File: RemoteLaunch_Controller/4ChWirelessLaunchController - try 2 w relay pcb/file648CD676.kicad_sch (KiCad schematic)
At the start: 24 parts, among them J1 Pad power and switch, J2 Control board, J3 Pad ch 1, J4 Pad ch 2, J5 Pad ch 3, J6 Pad ch 4, J7 Armed siren, J8 LED/Buzzer Continuity indicat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, J9 LED power indicator, K1 G2RL-2-DC24, K2 Ch 1 relay, K3 G8N-1U-DC12, K4 G8N-1U-DC12, K5 G8N-1U-DC12

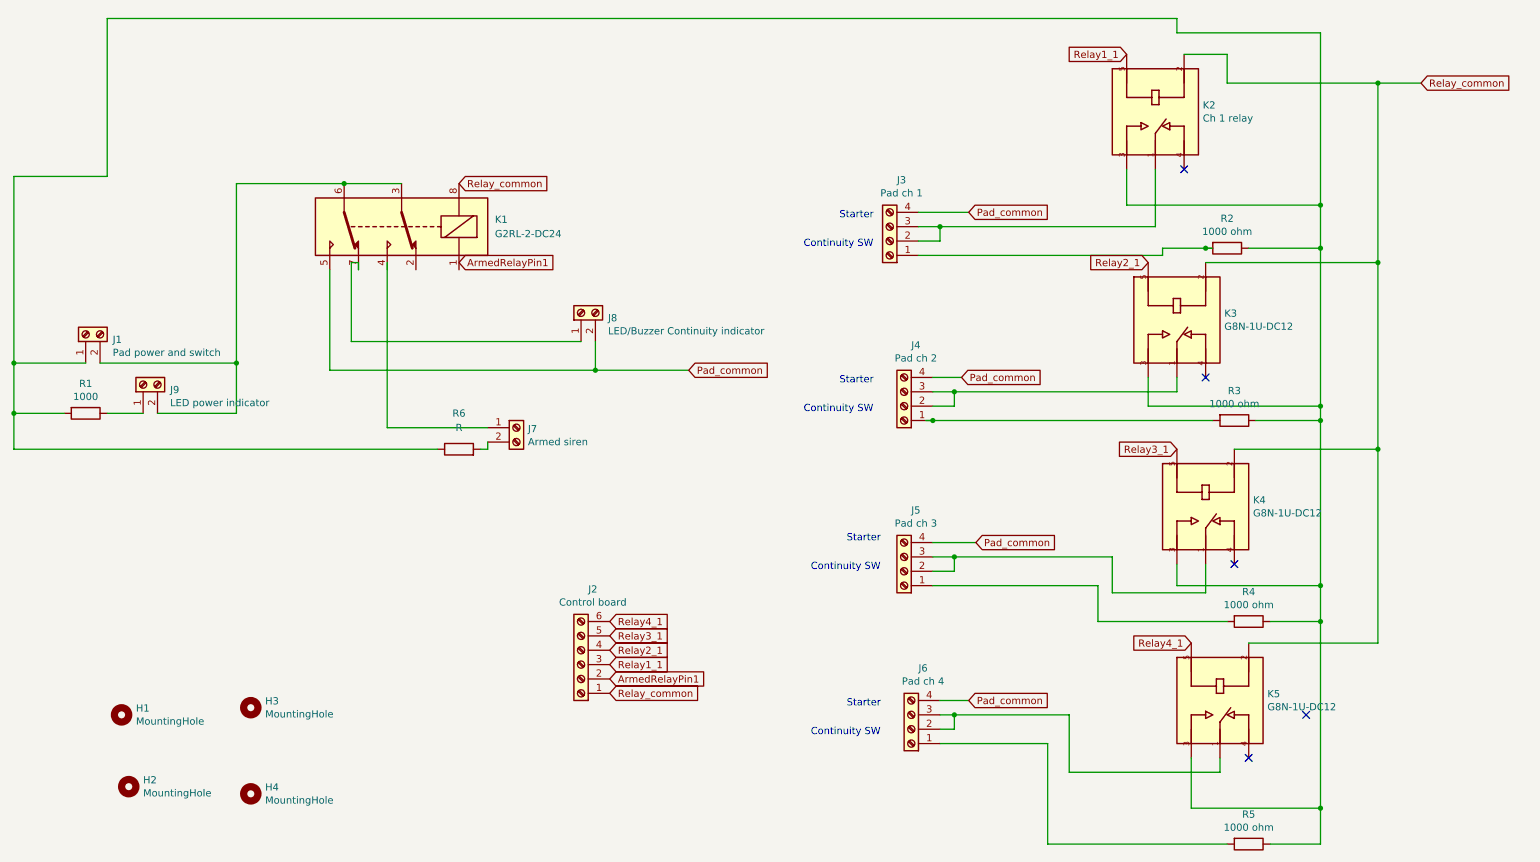
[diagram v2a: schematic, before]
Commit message: Working on adding polling / heartbeat;  Seem to have broken launch
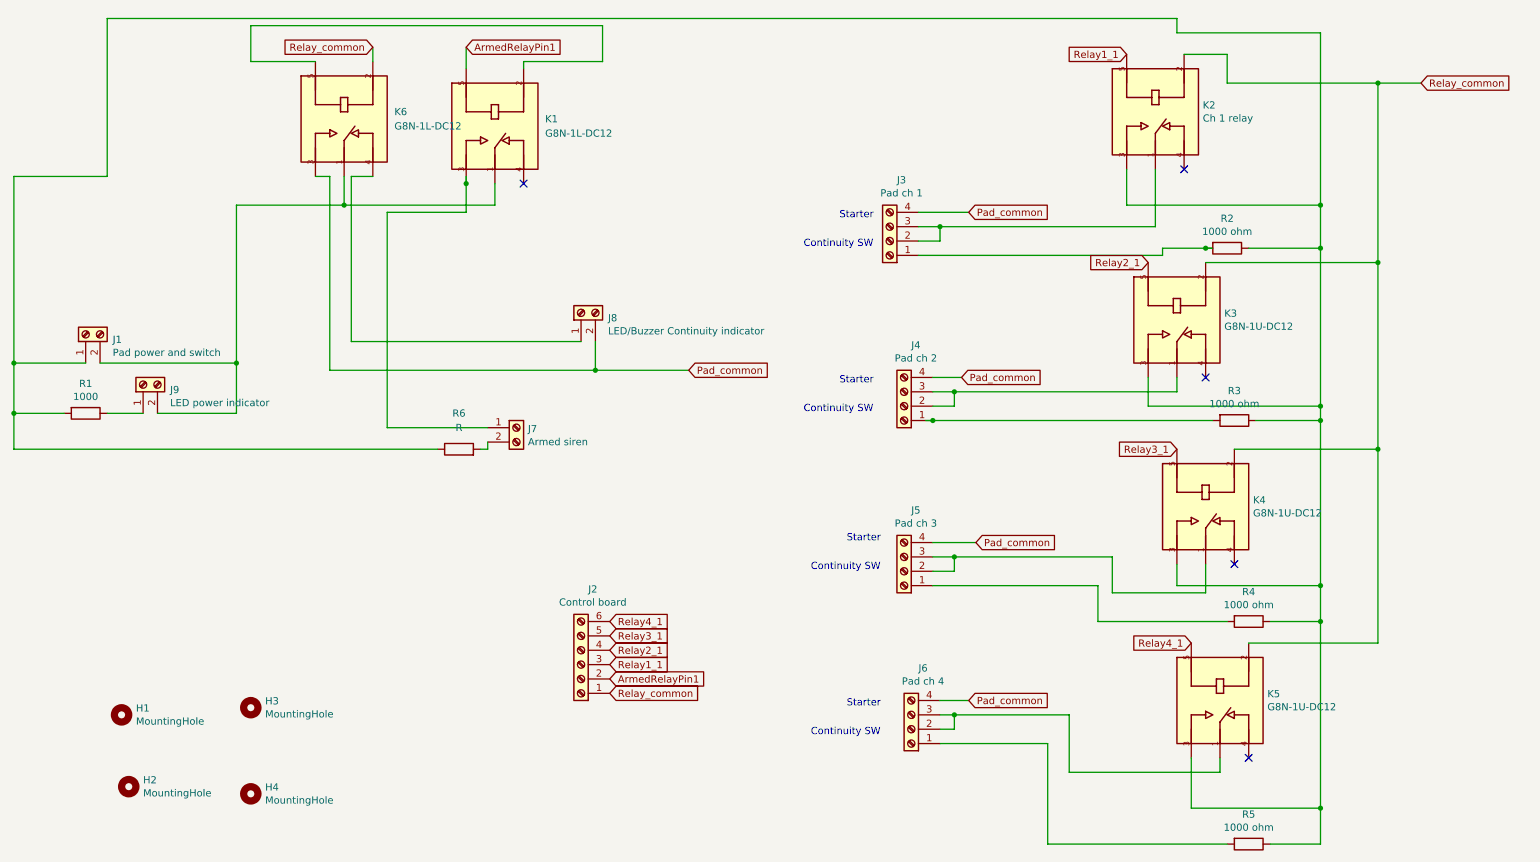
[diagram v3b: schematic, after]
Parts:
- removed K1: G2RL-2-DC24, Relay_THT:Relay_DPDT_Omron_G2RL, symbol Relay:G2RL-2-DC24
- added K1, K6: G8N-1L-DC12, RELAY_G8N-1U-DC12, symbol 4ChWirelessLaunchController-rescue:G8N-1U-DC12-G8N-1U-DC12
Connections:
- net ArmedRelayPin1: now also K1.5
- net Pad_common: now also K6.3
- net Relay_common: now also K6.2
- net at J1.2 (Pin_2), J9.2 (Pin_2): now also K1.1, K6.1
- net at J7.1 (Pin_1): now also K1.3
- net at J8.1 (Pin_1): now also K6.4
- new net: K1.2, K6.5
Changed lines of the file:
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@@
   (junction (at 255.27 29.21) (diameter 0) (color 0 0 0 0)
   )
-  (junction (at 72.39 46.99) (diameter 0) (color 0 0 0 0)
+  (junction (at 72.39 50.8) (diameter 0) (color 0 0 0 0)
+  )
+  (junction (at 93.98 46.99) (diameter 0) (color 0 0 0 0)
   )
   (junction (at 245.11 118.11) (diameter 0) (color 0 0 0 0)
@@
   (no_connect (at 232.41 148.59))
   (no_connect (at 229.87 114.3))
-  (no_connect (at 242.57 140.97))
   (no_connect (at 224.79 81.28))
+  (no_connect (at 104.14 46.99))
   (no_connect (at 220.98 44.45))
   (wire (pts (xy 245.11 157.48) (xy 245.11 163.83))
@@
     (stroke (width 0) (type default))
   )
+  (wire (pts (xy 77.47 22.86) (xy 77.47 25.4))
+    (stroke (width 0) (type default))
+  )
   (wire (pts (xy 13.97 78.74) (xy 13.97 87.63))
     (stroke (width 0) (type default))
@@
     (stroke (width 0) (type default))
   )
+  (wire (pts (xy 73.66 45.72) (xy 77.47 45.72))
+    (stroke (width 0) (type default))
+  )
   (wire (pts (xy 255.27 29.21) (xy 262.89 29.21))
     (stroke (width 0) (type default))
@@
     (stroke (width 0) (type default))
   )
+  (wire (pts (xy 67.31 25.4) (xy 55.88 25.4))
+    (stroke (width 0) (type default))
+  )
   (wire (pts (xy 228.6 24.13) (xy 228.6 29.21))
     (stroke (width 0) (type default))
@@
     (stroke (width 0) (type default))
   )
-  (wire (pts (xy 72.39 46.99) (xy 82.55 46.99))
+  (wire (pts (xy 93.98 46.99) (xy 93.98 52.07))
+    (stroke (width 0) (type default))
+  )
+  (wire (pts (xy 55.88 25.4) (xy 55.88 19.05))
     (stroke (width 0) (type default))
   )
@@
     (stroke (width 0) (type default))
   )
+  (wire (pts (xy 99.06 46.99) (xy 99.06 50.8))
+    (stroke (width 0) (type default))
+  )
   (wire (pts (xy 176.53 110.49) (xy 184.15 110.49))
     (stroke (width 0) (type default))
@@
     (stroke (width 0) (type default))
   )
+  (wire (pts (xy 55.88 19.05) (xy 118.11 19.05))
+    (stroke (width 0) (type default))
+  )
+  (wire (pts (xy 93.98 22.86) (xy 93.98 26.67))
+    (stroke (width 0) (type default))
+  )
   (wire (pts (xy 232.41 128.27) (xy 255.27 128.27))
     (stroke (width 0) (type default))
   )
-  (wire (pts (xy 73.66 60.96) (xy 73.66 74.93))
-    (stroke (width 0) (type default))
-  )
-  (wire (pts (xy 73.66 60.96) (xy 74.93 60.96))
+  (wire (pts (xy 73.66 45.72) (xy 73.66 74.93))
     (stroke (width 0) (type default))
   )
@@
     (stroke (width 0) (type default))
   )
+  (wire (pts (xy 72.39 45.72) (xy 72.39 50.8))
+    (stroke (width 0) (type default))
+  )
   (wire (pts (xy 245.11 86.36) (xy 245.11 88.9))
     (stroke (width 0) (type default))
@@
     (stroke (width 0) (type default))
   )
-  (wire (pts (xy 74.93 60.96) (xy 74.93 62.23))
-    (stroke (width 0) (type default))
-  )
-  (wire (pts (xy 69.85 62.23) (xy 69.85 80.01))
+  (wire (pts (xy 104.14 25.4) (xy 104.14 26.67))
+    (stroke (width 0) (type default))
+  )
+  (wire (pts (xy 69.85 45.72) (xy 69.85 80.01))
     (stroke (width 0) (type default))
   )
@@
     (stroke (width 0) (type default))
   )
-  (wire (pts (xy 53.34 46.99) (xy 72.39 46.99))
+  (wire (pts (xy 93.98 45.72) (xy 93.98 46.99))
+    (stroke (width 0) (type default))
+  )
+  (wire (pts (xy 53.34 50.8) (xy 72.39 50.8))
     (stroke (width 0) (type default))
   )
@@
     (stroke (width 0) (type default))
   )
+  (wire (pts (xy 118.11 25.4) (xy 104.14 25.4))
+    (stroke (width 0) (type default))
+  )
   (wire (pts (xy 205.74 124.46) (xy 228.6 124.46))
     (stroke (width 0) (type default))
@@
     (stroke (width 0) (type default))
   )
-  (wire (pts (xy 80.01 60.96) (xy 80.01 90.17))
+  (wire (pts (xy 80.01 52.07) (xy 80.01 90.17))
+    (stroke (width 0) (type default))
+  )
+  (wire (pts (xy 118.11 19.05) (xy 118.11 25.4))
     (stroke (width 0) (type default))
   )
@@
     (stroke (width 0) (type default))
   )
+  (wire (pts (xy 69.85 45.72) (xy 67.31 45.72))
+    (stroke (width 0) (type default))
+  )
   (wire (pts (xy 176.53 86.36) (xy 180.34 86.36))
     (stroke (width 0) (type default))
@@
     (stroke (width 0) (type default))
   )
+  (wire (pts (xy 80.01 52.07) (xy 93.98 52.07))
+    (stroke (width 0) (type default))
+  )
   (wire (pts (xy 13.97 45.72) (xy 30.48 45.72))
     (stroke (width 0) (type default))
@@
     (stroke (width 0) (type default))
   )
+  (wire (pts (xy 72.39 50.8) (xy 99.06 50.8))
+    (stroke (width 0) (type default))
+  )
   (wire (pts (xy 13.97 93.98) (xy 88.9 93.98))
     (stroke (width 0) (type default))
@@
     (stroke (width 0) (type default))
   )
-  (wire (pts (xy 53.34 46.99) (xy 53.34 78.74))
+  (wire (pts (xy 53.34 50.8) (xy 53.34 78.74))
     (stroke (width 0) (type default))
   )
@@
     )
   )
-  (global_label "ArmedRelayPin1" (shape input) (at 92.71 60.96 0)
+  (global_label "ArmedRelayPin1" (shape input) (at 93.98 22.86 0)
     (effects (font (size 1.27 1.27)) (justify left))
-    (property "Intersheetrefs" "${INTERSHEET_REFS}" (at 92.71 60.96 0)
+    (property "Intersheetrefs" "${INTERSHEET_REFS}" (at 93.98 22.86 0)
       (effects (font (size 1.27 1.27)) hide)
     )
@@
     )
   )
-  (global_label "Relay_common" (shape input) (at 92.71 46.99 0)
-    (effects (font (size 1.27 1.27)) (justify left))
-    (property "Intersheetrefs" "${INTERSHEET_REFS}" (at 92.71 46.99 0)
+  (global_label "Relay_common" (shape input) (at 77.47 22.86 180)
+    (effects (font (size 1.27 1.27)) (justify right))
+    (property "Intersheetrefs" "${INTERSHEET_REFS}" (at 77.47 22.86 0)
       (effects (font (size 1.27 1.27)) hide)
     )
@@
     )
   )
+  (symbol (lib_id "4ChWirelessLaunchController-rescue:G8N-1U-DC12-G8N-1U-DC12") (at 99.06 36.83 270) (unit 1)
+    (in_bom yes) (on_board yes) (dnp no) (fields_autoplaced)
+    (property "Reference" "K1" (at 107.95 35.56 90)
+      (effects (font (size 1.27 1.27)) (justify left))
+    )
+    (property "Value" "G8N-1L-DC12" (at 107.95 38.1 90)
+      (effects (font (size 1.27 1.27)) (justify left))
+    )
+    (property "Footprint" "RELAY_G8N-1U-DC12" (at 99.06 36.83 0)
+      (effects (font (size 1.27 1.27)) (justify left bottom) hide)
+    )
+    (property "Datasheet" "" (at 99.06 36.83 0)
+      (effects (font (size 1.27 1.27)) (justify left bottom) hide)
+    )
+    (property "PARTREV" "NA" (at 99.06 36.83 0)
+      (effects (font (size 1.27 1.27)) (justify left bottom) hide)
+    )
+    (property "STANDARD" "Manufacturer Recommendations" (at 99.06 36.83 0)
+      (effects (font (size 1.27 1.27)) (justify left bottom) hide)
+    )
+    (property "MAXIMUM_PACKAGE_HEIGHT" "13.8mm" (at 99.06 36.83 0)
+      (effects (font (size 1.27 1.27)) (justify left bottom) hide)
+    )
+    (property "MANUFACTURER" "Omron" (at 99.06 36.83 0)
+      (effects (font (size 1.27 1.27)) (justify left bottom) hide)
+    )
+    (pin "1")
+    (pin "2")
+    (pin "3")
+    (pin "4")
+    (pin "5")
+    (instances
+      (project "4ChWirelessLaunchController"
+        (path "/eeec8993-d09e-49cb-a9f8-4cbca24d477a/00000000-0000-0000-0000-0000648cd677"
+          (reference "K1") (unit 1)
+        )
+      )
+    )
+  )
   (symbol (lib_id "Device:R") (at 92.71 93.98 90) (unit 1)
     (in_bom yes) (on_board yes) (dnp no) (fields_autoplaced)
@@
     )
   )
-  (symbol (lib_id "Relay:G2RL-2-DC24") (at 82.55 54.61 180) (unit 1)
+  (symbol (lib_id "4ChWirelessLaunchController-rescue:G8N-1U-DC12-G8N-1U-DC12") (at 72.39 35.56 270) (unit 1)
     (in_bom yes) (on_board yes) (dnp no) (fields_autoplaced)
-    (property "Reference" "K1" (at 99.06 53.34 0)
-      (effects (font (size 1.27 1.27)) (justify right))
-    )
-    (property "Value" "G2RL-2-DC24" (at 99.06 55.88 0)
-      (effects (font (size 1.27 1.27)) (justify right))
-    )
-    (property "Footprint" "Relay_THT:Relay_DPDT_Omron_G2RL" (at 66.04 53.34 0)
-      (effects (font (size 1.27 1.27)) (justify left) hide)
-    )
-    (property "Datasheet" "https://omronfs.omron.com/en_US/ecb/products/pdf/en-g2rl.pdf" (at 82.55 54.61 0)
-      (effects (font (size 1.27 1.27)) hide)
+    (property "Reference" "K6" (at 81.28 34.29 90)
+      (effects (font (size 1.27 1.27)) (justify left))
+    )
+    (property "Value" "G8N-1L-DC12" (at 81.28 36.83 90)
+      (effects (font (size 1.27 1.27)) (justify left))
+    )
+    (property "Footprint" "RELAY_G8N-1U-DC12" (at 72.39 35.56 0)
+      (effects (font (size 1.27 1.27)) (justify left bottom) hide)
+    )
+    (property "Datasheet" "" (at 72.39 35.56 0)
+      (effects (font (size 1.27 1.27)) (justify left bottom) hide)
+    )
+    (property "PARTREV" "NA" (at 72.39 35.56 0)
+      (effects (font (size 1.27 1.27)) (justify left bottom) hide)
+    )
+    (property "STANDARD" "Manufacturer Recommendations" (at 72.39 35.56 0)
+      (effects (font (size 1.27 1.27)) (justify left bottom) hide)
+    )
+    (property "MAXIMUM_PACKAGE_HEIGHT" "13.8mm" (at 72.39 35.56 0)
+      (effects (font (size 1.27 1.27)) (justify left bottom) hide)
+    )
+    (property "MANUFACTURER" "Omron" (at 72.39 35.56 0)
+      (effects (font (size 1.27 1.27)) (justify left bottom) hide)
     )
     (pin "1")
@@
     (pin "4")
     (pin "5")
-    (pin "6")
-    (pin "7")
-    (pin "8")
-    (instances
-      (project "4ChWirelessLaunchController"
-        (path "/eeec8993-d09e-49cb-a9f8-4cbca24d477a/00000000-0000-0000-0000-0000648cd677"
-          (reference "K1") (unit 1)
-        )
-      )
+    (instances
+      (project "4ChWirelessLaunchController"
+        (path "/eeec8993-d09e-49cb-a9f8-4cbca24d477a/00000000-0000-0000-0000-0000648cd677"
+          (reference "K6") (unit 1)
+        )
+      )
